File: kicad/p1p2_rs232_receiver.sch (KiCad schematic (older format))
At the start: 46 parts, among them J101 TE Connectivity 1776112-3, J102 USB_B_Mini, Q101 Q_NPN_CBE, U101 MAX22088, U102 ISO7342C, U103 CY7C65213-32LTXI

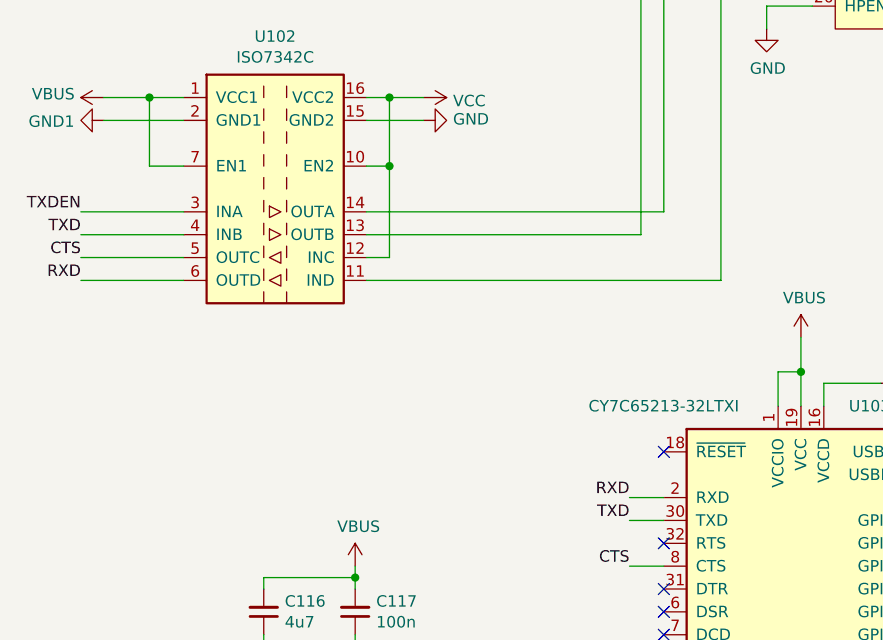
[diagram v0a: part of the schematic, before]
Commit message: Add 9600baud CTS low pass filter
- Add low pass filter with tRC of 1.2 msec
- Pull CTS low when data is received for easy collision detection

Signed-off-by: Patrick Rudolph <siro@das-labor.org>
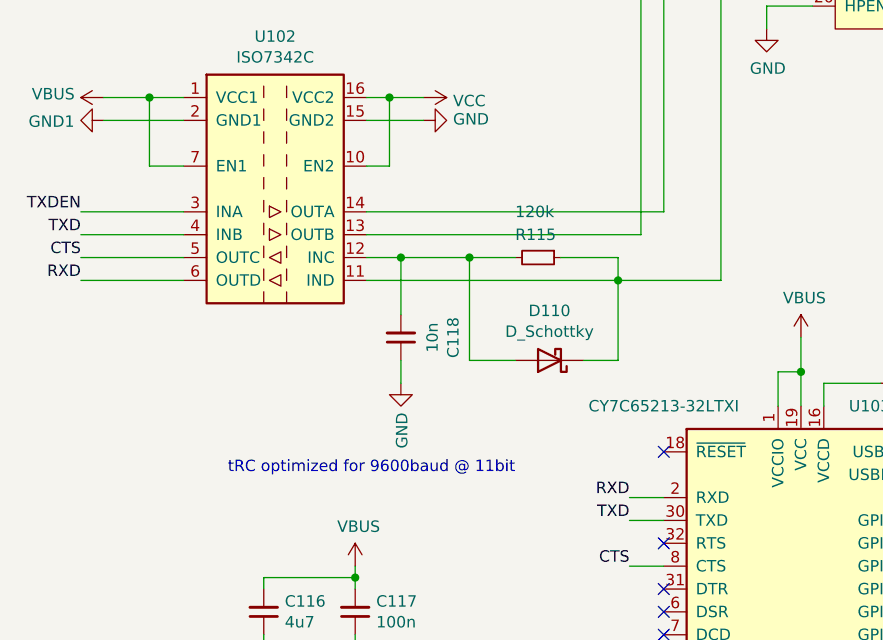
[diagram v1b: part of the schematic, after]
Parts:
- added C118: 10n, Capacitor_SMD:C_0805_2012Metric_Pad1.18x1.45mm_HandSolder, symbol Device:C_Small
- added D110: D_Schottky, Diode_SMD:D_SOD-123, symbol Device:D_Schottky
- added R115: 120k, Resistor_SMD:R_0805_2012Metric_Pad1.20x1.40mm_HandSolder, symbol Device:R_Small
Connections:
- net GND: now also C118.1
- net VCC: no longer U102.12 (INC)
- net at U101.1 (DOUT), U102.11 (IND): now also D110.1 (K), R115.1
- new net: C118.2, D110.2 (A), R115.2, U102.12 (INC)
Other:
- note added: "tRC optimized for 9600baud @ 11bit"
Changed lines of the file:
@@
 	2750 3600 2650 3600
 Wire Wire Line
-	2650 4400 4200 4400
+	2650 4400 3750 4400
 Wire Wire Line
 	7500 1700 7400 1700
@@
 Wire Notes Line
 	7800 1150 6650 1150
-Wire Wire Line
-	2650 4300 2750 4300
-Wire Wire Line
-	2750 4300 2750 3900
-Connection ~ 2750 3900
 $Comp
 L Device:LED D104
@@
 Wire Wire Line
 	1700 3900 1850 3900
+$Comp
+L Device:C_Small C118
+U 1 1 61385EAB
+P 2800 4650
+F 0 "C118" V 2571 4650 50  0000 C CNN
+F 1 "10n" V 2662 4650 50  0000 C CNN
+F 2 "Capacitor_SMD:C_0805_2012Metric_Pad1.18x1.45mm_HandSolder" H 2800 4650 50  0001 C CNN
+F 3 "~" H 2800 4650 50  0001 C CNN
+	1    2800 4650
+	-1   0    0    1
+$EndComp
+$Comp
+L power:GND #PWR0133
+U 1 1 613863F9
+P 2800 4850
+F 0 "#PWR0133" H 2800 4600 50  0001 C CNN
+F 1 "GND" V 2805 4722 50  0000 R CNN
+F 2 "" H 2800 4850 50  0001 C CNN
+F 3 "" H 2800 4850 50  0001 C CNN
+	1    2800 4850
+	1    0    0    -1
+$EndComp
+Wire Wire Line
+	2800 4850 2800 4750
+Wire Wire Line
+	2800 4550 2800 4300
+Wire Wire Line
+	2800 4300 2650 4300
+$Comp
+L Device:R_Small R115
+U 1 1 6139F506
+P 3400 4300
+F 0 "R115" V 3300 4200 50  0000 L CNN
+F 1 "120k" V 3200 4200 50  0000 L CNN
+F 2 "Resistor_SMD:R_0805_2012Metric_Pad1.20x1.40mm_HandSolder" H 3400 4300 50  0001 C CNN
+F 3 "~" H 3400 4300 50  0001 C CNN
+	1    3400 4300
+	0    1    1    0
+$EndComp
+Wire Wire Line
+	3300 4300 3100 4300
+Connection ~ 2800 4300
+Wire Wire Line
+	3500 4300 3750 4300
+Wire Wire Line
+	3750 4300 3750 4400
+Connection ~ 3750 4400
+$Comp
+L Device:D_Schottky D110
+U 1 1 613BA204
+P 3450 4750
+F 0 "D110" H 3450 4533 50  0000 C CNN
+F 1 "D_Schottky" H 3450 4624 50  0000 C CNN
+F 2 "Diode_SMD:D_SOD-123" H 3450 4750 50  0001 C CNN
+F 3 "~" H 3450 4750 50  0001 C CNN
+	1    3450 4750
+	-1   0    0    1
+$EndComp
+Wire Wire Line
+	3600 4750 3750 4750
+Wire Wire Line
+	3750 4750 3750 4400
+Wire Wire Line
+	3750 4400 4200 4400
+Wire Wire Line
+	3300 4750 3100 4750
+Wire Wire Line
+	3100 4750 3100 4300
+Connection ~ 3100 4300
+Wire Wire Line
+	3100 4300 2800 4300
+Text Notes 3300 5250 2    50   ~ 0
+tRC optimized for 9600baud @ 11bit
 $EndSCHEMATC

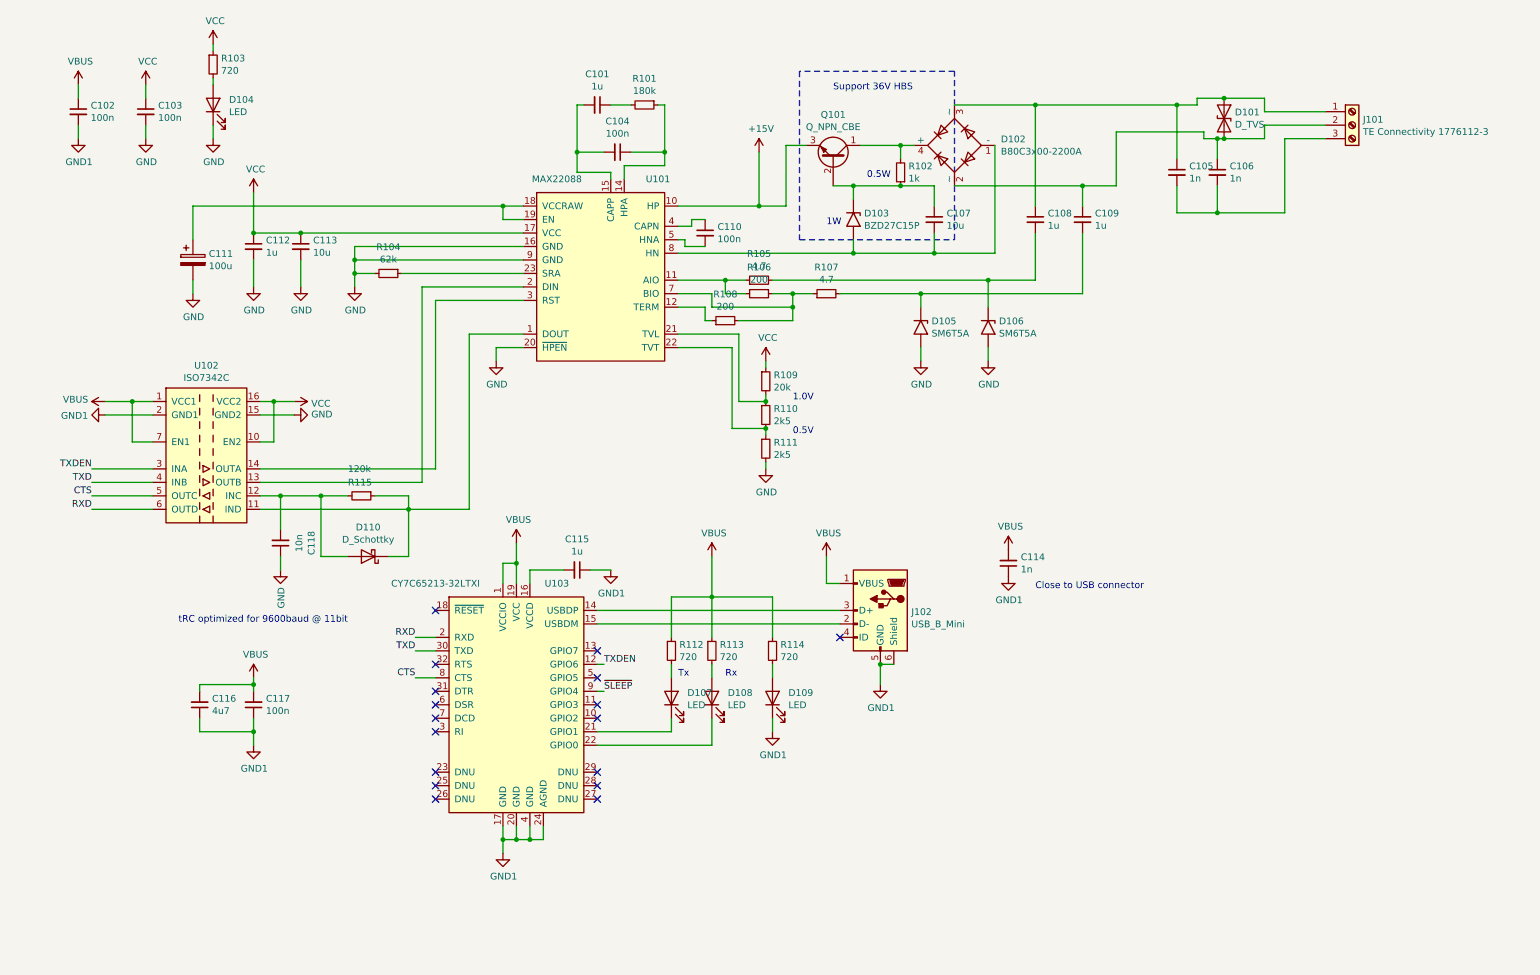
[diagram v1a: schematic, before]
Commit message: pcb: Place Arduino on board
Add an Arduino to the board and a connector for external microcontrollers.
The HBS protocol requires AMI code to be transmitted, which cannot be easily
be done in hardware due to clock recovery issues.

Signed-off-by: Patrick Rudolph <siro@das-labor.org>
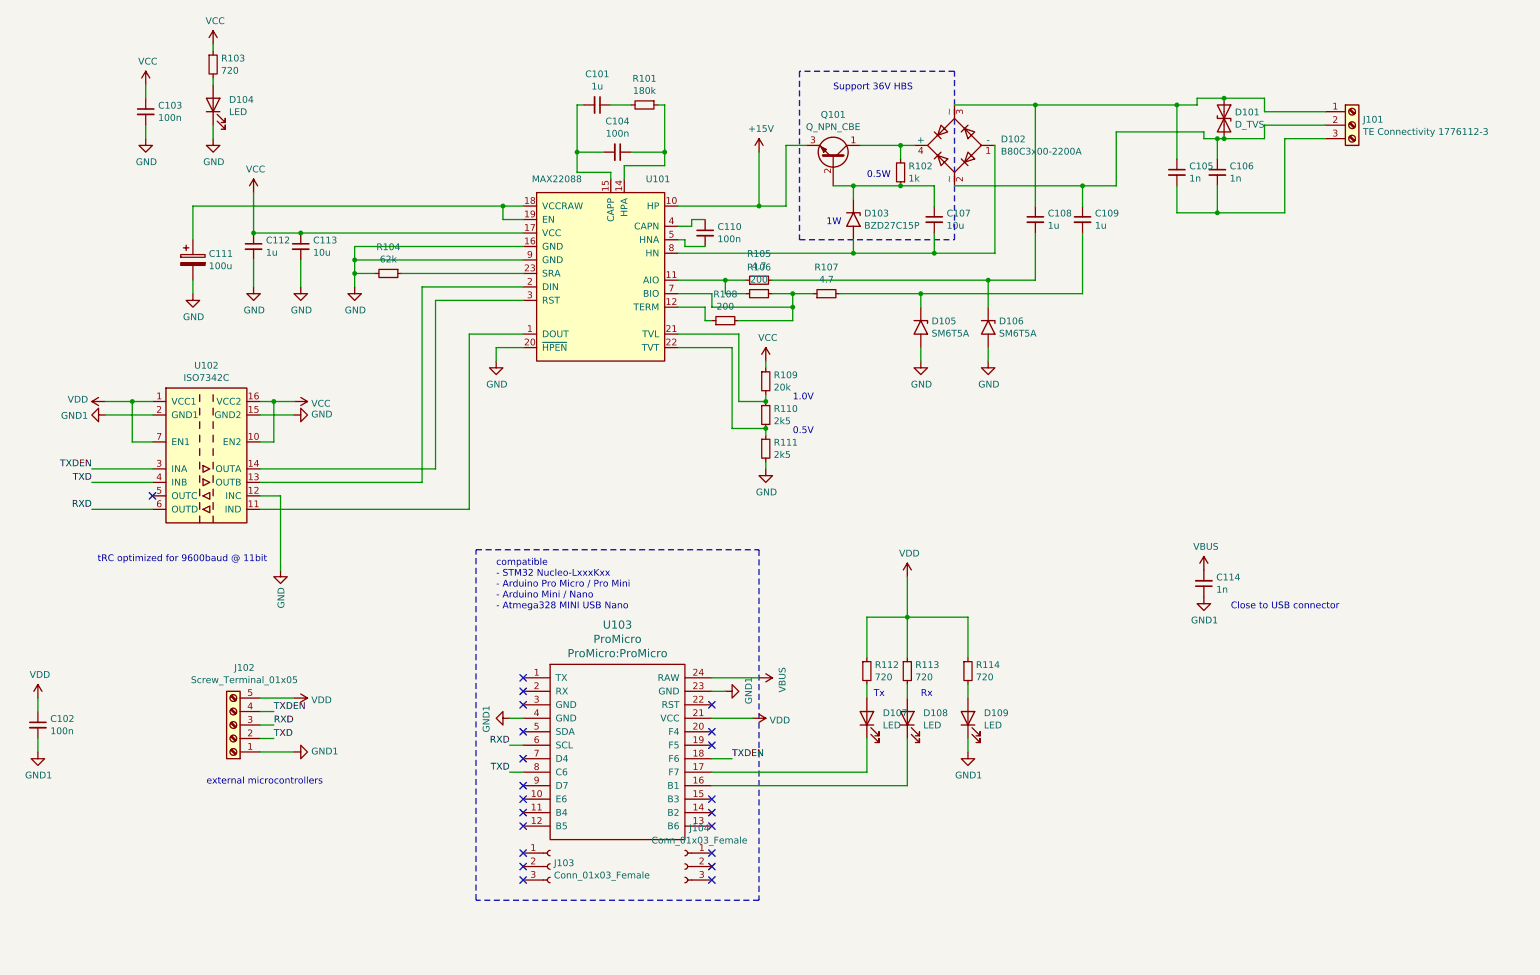
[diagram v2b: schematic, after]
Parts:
- removed C115: 1u, Capacitor_SMD:C_1210_3225Metric_Pad1.33x2.70mm_HandSolder, symbol Device:C_Small
- removed C116: 4u7, Capacitor_SMD:C_1210_3225Metric_Pad1.33x2.70mm_HandSolder, symbol Device:C_Small
- removed C117: 100n, Capacitor_SMD:C_0805_2012Metric_Pad1.18x1.45mm_HandSolder, symbol Device:C_Small
- removed C118: 10n, Capacitor_SMD:C_0805_2012Metric_Pad1.18x1.45mm_HandSolder, symbol Device:C_Small
- removed D110: D_Schottky, Diode_SMD:D_SOD-123, symbol Device:D_Schottky
- removed J102: USB_B_Mini, Connector_USB:USB_Mini-B_Wuerth_65100516121_Horizontal, symbol Connector:USB_B_Mini
- removed R115: 120k, Resistor_SMD:R_0805_2012Metric_Pad1.20x1.40mm_HandSolder, symbol Device:R_Small
- removed U103: CY7C65213-32LTXI, Package_DFN_QFN:QFN-32-1EP_5x5mm_P0.5mm_EP3.45x3.45mm, symbol Interface_USB:CY7C65213-32LTXI
- added J102: Screw_Terminal_01x05, TerminalBlock_MetzConnect:TerminalBlock_MetzConnect_Type059_RT06305HBWC_1x05_P3.50mm_Horizontal, symbol Connector:Screw_Terminal_01x05
- added J103, J104: Conn_01x03_Female, Connector_PinSocket_2.54mm:PinSocket_1x03_P2.54mm_Vertical, symbol Connector:Conn_01x03_Female
- added U103: ProMicro, ProMicro:ProMicro, symbol ProMicro:ProMicro
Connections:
- net GND: now also U102.12 (INC)
- net GND1: now also J102.1 (Pin_1), U103.23 (GND), U103.4 (GND)
- net RXD: now also J102.3 (Pin_3), U103.6 (SCL)
- net TXD: now also J102.2 (Pin_2), U103.8 (C6)
- net TXDEN: now also J102.4 (Pin_4), U103.18 (F6)
- net VBUS: now also U103.24 (RAW); no longer C102.1, R112.1, R113.1, R114.1, U102.1 (VCC1), U102.7 (EN1)
- net at D107.1 (K): now also U103.17 (F7)
- net at D108.1 (K): now also U103.16 (B1)
- net CTS: no longer names the net of U102.5 (OUTC)
- new net VDD: C102.1, J102.5 (Pin_5), R112.1, R113.1, R114.1, U102.1 (VCC1), U102.7 (EN1), U103.21 (VCC)
- no-connect marks 17 -> 22
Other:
- note added: "compatible\n- STM32 Nucleo-LxxxKxx\n- Arduino Pro Micro / Pro Mini\n- Arduino Mini / Nano\n- Atmega328 MINI USB Nano"
- note added: "external microcontrollers"
- moved on the sheet: C102, C114, D107, D108, D109, R112, R113, R114

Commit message: Fix some issues
- Fix Q101 pinout
- Change 2k5 to 2k49 Ohm
- Change 720 to 750 Ohm

Signed-off-by: Patrick Rudolph <siro@das-labor.org>
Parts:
- removed Q101: Q_NPN_CBE, Package_TO_SOT_SMD:SOT-223, symbol Device:Q_NPN_CBE
- added Q101: Q_NPN_BCE, Package_TO_SOT_SMD:SOT-223-3_TabPin2, symbol Device:Q_NPN_BCE
- R103, R112, R113, R114: value 720 -> 750
- R110, R111: value 2k5 -> 2k49
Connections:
- net +15V: now also Q101.3 (E)
- net at D102.4 (+), R102.2: now also Q101.2 (C)
- net at C107.1, D103.1 (A1), R102.1: now also Q101.1 (B)
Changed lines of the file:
@@
 P 6400 3950
 F 0 "R111" H 6459 3996 50  0000 L CNN
-F 1 "2k5" H 6459 3905 50  0000 L CNN
+F 1 "2k49" H 6459 3905 50  0000 L CNN
 F 2 "Resistor_SMD:R_0805_2012Metric_Pad1.20x1.40mm_HandSolder" H 6400 3950 50  0001 C CNN
 F 3 "~" H 6400 3950 50  0001 C CNN
@@
 P 6400 3700
 F 0 "R110" H 6459 3746 50  0000 L CNN
-F 1 "2k5" H 6459 3655 50  0000 L CNN
+F 1 "2k49" H 6459 3655 50  0000 L CNN
 F 2 "Resistor_SMD:R_0805_2012Metric_Pad1.20x1.40mm_HandSolder" H 6400 3700 50  0001 C CNN
 F 3 "~" H 6400 3700 50  0001 C CNN
@@
 P 7150 5600
 F 0 "R112" H 7209 5646 50  0000 L CNN
-F 1 "720" H 7209 5555 50  0000 L CNN
+F 1 "750" H 7209 5555 50  0000 L CNN
 F 2 "Resistor_SMD:R_0805_2012Metric_Pad1.20x1.40mm_HandSolder" H 7150 5600 50  0001 C CNN
 F 3 "~" H 7150 5600 50  0001 C CNN
@@
 P 7450 5600
 F 0 "R113" H 7509 5646 50  0000 L CNN
-F 1 "720" H 7509 5555 50  0000 L CNN
+F 1 "750" H 7509 5555 50  0000 L CNN
 F 2 "Resistor_SMD:R_0805_2012Metric_Pad1.20x1.40mm_HandSolder" H 7450 5600 50  0001 C CNN
 F 3 "~" H 7450 5600 50  0001 C CNN
@@
 P 7900 5600
 F 0 "R114" H 7959 5646 50  0000 L CNN
-F 1 "720" H 7959 5555 50  0000 L CNN
+F 1 "750" H 7959 5555 50  0000 L CNN
 F 2 "Resistor_SMD:R_0805_2012Metric_Pad1.20x1.40mm_HandSolder" H 7900 5600 50  0001 C CNN
 F 3 "~" H 7900 5600 50  0001 C CNN
@@
 Wire Wire Line
 	7500 1700 7400 1700
-$Comp
-L Device:Q_NPN_CBE Q101
-U 1 1 615ECDC6
-P 6900 1800
-F 0 "Q101" V 7228 1800 50  0000 C CNN
-F 1 "Q_NPN_CBE" V 7137 1800 50  0000 C CNN
-F 2 "Package_TO_SOT_SMD:SOT-223" H 7100 1900 50  0001 C CNN
-F 3 "~" H 6900 1800 50  0001 C CNN
-	1    6900 1800
-	0    1    -1   0
-$EndComp
 $Comp
 L Device:R_Small R102
@@
 P 2300 1100
 F 0 "R103" H 2359 1146 50  0000 L CNN
-F 1 "720" H 2359 1055 50  0000 L CNN
+F 1 "750" H 2359 1055 50  0000 L CNN
 F 2 "Resistor_SMD:R_0805_2012Metric_Pad1.20x1.40mm_HandSolder" H 2300 1100 50  0001 C CNN
 F 3 "~" H 2300 1100 50  0001 C CNN
@@
 Wire Notes Line
 	4250 4700 6350 4700
+$Comp
+L Device:Q_NPN_BCE Q101
+U 1 1 61576D06
+P 6900 1800
+F 0 "Q101" V 7228 1800 50  0000 C CNN
+F 1 "Q_NPN_BCE" V 7137 1800 50  0000 C CNN
+F 2 "Package_TO_SOT_SMD:SOT-223-3_TabPin2" H 7100 1900 50  0001 C CNN
+F 3 "~" H 6900 1800 50  0001 C CNN
+	1    6900 1800
+	0    1    -1   0
+$EndComp
 $EndSCHEMATC
